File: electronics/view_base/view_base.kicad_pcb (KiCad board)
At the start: 2 copper layers, 81.2 x 81.2 mm, 111 parts, among them J1 BLDC, J2 USB_C_Receptacle_USB2.0, J3 LCD, J4 A, J5 B, J6 Conn_01x28_Socket, J7 Conn_01x28_Socket, J8 Conn_01x03_Socket, J9 Conn_01x04_Socket, Q1 MMBT4403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

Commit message: sunday work
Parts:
- moved J8 229.9 mm to (88.5, 192.0)
- moved J6 193.5 mm to (71.0, 155.8)
- moved J7 193.5 mm to (75.6, 155.8)
- moved J9 191.9 mm to (102.5, 153.0)
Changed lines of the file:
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@@
 		(legacy_teardrops no)
 	)
-	(paper "A4")
+	(paper "A3")
 	(layers
 		(0 "F.Cu" signal)
@@
 	(footprint "Connector_PinSocket_2.54mm:PinSocket_1x28_P2.54mm_Vertical"
 		(layer "F.Cu")
-		(at 66.2 -37.58)
+		(at 71 155.84)
 		(descr "Through hole straight socket strip, 1x28, 2.54mm pitch, single row (from Kicad 4.0.7), script generated")
 		(tags "Through hole socket strip THT 1x28 2.54mm single row")
@@
 	(footprint "Connector_PinSocket_2.54mm:PinSocket_1x28_P2.54mm_Vertical"
 		(layer "F.Cu")
-		(at 70.8 -37.58)
+		(at 75.6 155.84)
 		(descr "Through hole straight socket strip, 1x28, 2.54mm pitch, single row (from Kicad 4.0.7), script generated")
 		(tags "Through hole socket strip THT 1x28 2.54mm single row")
@@
 	(footprint "Connector_PinSocket_2.54mm:PinSocket_1x03_P2.54mm_Vertical"
 		(layer "F.Cu")
-		(at 75.4 -37.58)
+		(at 88.5 191.96)
 		(descr "Through hole straight socket strip, 1x03, 2.54mm pitch, single row (from Kicad 4.0.7), script generated")
 		(tags "Through hole socket strip THT 1x03 2.54mm single row")
@@
 	(footprint "Connector_PinSocket_2.54mm:PinSocket_1x04_P2.54mm_Vertical"
 		(layer "F.Cu")
-		(at 80 -37.58)
+		(at 102.5 152.96)
 		(descr "Through hole straight socket strip, 1x04, 2.54mm pitch, single row (from Kicad 4.0.7), script generated")
 		(tags "Through hole socket strip THT 1x04 2.54mm single row")
@@
 	(gr_arc
 		(start 103.499999 116.00781)
-		(mid 103.605914 115.700081)
+		(mid 103.60591 115.700076)
 		(end 103.878787 115.522725)
 		(stroke
@@
 	(gr_arc
 		(start 114.716361 102.903226)
-		(mid 114.889406 102.613745)
+		(mid 114.889406 102.613747)
 		(end 115.206906 102.5)
 		(stroke
@@
 	(gr_arc
 		(start 115.522726 103.878787)
-		(mid 115.700082 103.605915)
+		(mid 115.700083 103.605919)
 		(end 116.00781 103.5)
 		(stroke
@@
 	(gr_arc
 		(start 123.290199 96.500001)
-		(mid 123.790199 97.000001)
+		(mid 123.790199 97)
 		(end 123.290199 97.500001)
 		(stroke
@@
 	(gr_arc
 		(start 106.999999 97.250001)
-		(mid 107.219669 96.719671)
+		(mid 107.219668 96.71967)
 		(end 107.749999 96.500001)
 		(stroke
@@
 	(gr_arc
 		(start 107.749999 103.5)
-		(mid 107.219669 103.28033)
+		(mid 107.21967 103.28033)
 		(end 106.999999 102.75)
 		(stroke
@@
 	(gr_arc
 		(start 115.206906 97.500002)
-		(mid 114.889405 97.386257)
+		(mid 114.889401 97.38626)
 		(end 114.71636 97.096775)
 		(stroke
@@
 	(gr_arc
 		(start 102.499998 115.206906)
-		(mid 102.613743 114.889405)
+		(mid 102.61374 114.889401)
 		(end 102.903225 114.71636)
 		(stroke
@@
 	(gr_arc
 		(start 140.6 136.599999)
-		(mid 139.428427 139.428426)
+		(mid 139.428427 139.428427)
 		(end 136.6 140.599999)
 		(stroke
@@
 	(gr_arc
 		(start 76.709801 103.499999)
-		(mid 76.209801 102.999999)
+		(mid 76.209801 103)
 		(end 76.709801 102.499999)
 		(stroke
@@
 	(gr_arc
 		(start 83.99219 103.499999)
-		(mid 84.299919 103.605914)
+		(mid 84.299924 103.60591)
 		(end 84.477275 103.878787)
 		(stroke
@@
 	(gr_arc
 		(start 97.096774 114.71636)
-		(mid 97.386256 114.889405)
+		(mid 97.386254 114.889406)
 		(end 97.500001 115.206906)
 		(stroke
@@
 	(gr_arc
 		(start 84.793094 102.499998)
-		(mid 85.110595 102.613743)
+		(mid 85.110599 102.61374)
 		(end 85.28364 102.903225)
 		(stroke
@@
 	(gr_arc
 		(start 102.903226 85.283639)
-		(mid 102.613745 85.110594)
+		(mid 102.613747 85.110594)
 		(end 102.5 84.793094)
 		(stroke
@@
 	(gr_arc
 		(start 123.290199 102.5)
-		(mid 123.790199 103)
+		(mid 123.7902 103)
 		(end 123.290199 103.5)
 		(stroke
@@
 	(gr_arc
 		(start 96.121213 115.522726)
-		(mid 96.394085 115.700082)
+		(mid 96.394081 115.700083)
 		(end 96.5 116.00781)
 		(stroke
@@
 	(gr_arc
 		(start 97.500002 84.793094)
-		(mid 97.386257 85.110595)
+		(mid 97.38626 85.110599)
 		(end 97.096775 85.28364)
 		(stroke
@@
 	(gr_arc
 		(start 103.878787 84.477274)
-		(mid 103.605915 84.299918)
+		(mid 103.605919 84.299917)
 		(end 103.5 83.99219)
 		(stroke
@@
 	(gr_arc
 		(start 116.00781 96.500001)
-		(mid 115.700081 96.394086)
+		(mid 115.700076 96.39409)
 		(end 115.522725 96.121213)
 		(stroke
@@
 	(gr_arc
 		(start 96.500001 83.99219)
-		(mid 96.394086 84.299919)
+		(mid 96.39409 84.299924)
 		(end 96.121213 84.477275)
 		(stroke
@@
 	(gr_arc
 		(start 76.709801 97.5)
-		(mid 76.209801 97)
+		(mid 76.2098 97)
 		(end 76.709801 96.5)
 		(stroke
@@
 	(gr_arc
 		(start 85.283638 97.096775)
-		(mid 85.110593 97.386256)
+		(mid 85.110593 97.386253)
 		(end 84.793094 97.5)
 		(stroke
@@
 	(gr_arc
 		(start 84.477274 96.121213)
-		(mid 84.299918 96.394085)
+		(mid 84.299917 96.394081)
 		(end 83.99219 96.5)
 		(stroke

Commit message: initial layout
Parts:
- removed C28: 1uF, Capacitor_SMD:C_0603_1608Metric
- removed R17: 10k, Resistor_SMD:R_0603_1608Metric
- removed U2: T-Micro32_Plus, lilygo_micro32:T-Micro32
- moved J8 145.4 mm to (53.7, 50.8), turned to 180 degrees
- moved J9 119.8 mm to (35.9, 53.4), turned to 180 degrees
- moved J7 43.9 mm to (35.9, 137.2), turned to 180 degrees
- moved J6 25.5 mm to (53.7, 137.2), turned to 180 degrees
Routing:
- net /SCL: track 104.2 -> 0.00 mm, vias 4 -> 0
- net /GPIO12: track 0.00 -> 104.2 mm, vias 0 -> 4
- net /SDA: track 97.0 -> 0.00 mm, vias 3 -> 0
- net /GPIO13: track 0.00 -> 97.0 mm, vias 0 -> 3
- net /TMC_DIAG: track 85.9 -> 0.00 mm
- net /GPIO0: track 0.00 -> 85.9 mm
- net /TMC_VL: track 75.2 -> 0.00 mm, vias 2 -> 0
- net /GPIO1: track 0.00 -> 75.2 mm, vias 0 -> 2
- net /TMC_WL: track 71.5 -> 0.00 mm, vias 2 -> 0
- net /GPIO2: track 0.00 -> 71.5 mm, vias 0 -> 2
- net /TMC_UL: track 68.4 -> 0.00 mm, vias 2 -> 0
- net /GPIO3: track 0.00 -> 68.4 mm, vias 0 -> 2
- net /TMC_WH: track 68.0 -> 0.00 mm, vias 4 -> 0
- net /GPIO7: track 0.00 -> 68.0 mm, vias 0 -> 4
- net /TMC_VH: track 67.3 -> 0.00 mm, vias 4 -> 0
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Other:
- board size 81.2 x 81.2 mm -> 110.1 x 100 mm

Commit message: more layout and simplification
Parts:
- removed Q2: UMH3N, Package_TO_SOT_SMD:SOT-363_SC-70-6
- removed TP13: EN, Modified:TestPoint_Pad_D2.0mm_ValueSilk
- removed TP14: BOOT, Modified:TestPoint_Pad_D2.0mm_ValueSilk
- moved C26 45.3 mm to (58.0, 73.0), turned to 90 degrees
- moved J3 41.1 mm to (58.0, 79.0)
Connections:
- J6 pad 18: /ESP32_BOOT -> /GPIO15
- R12 pad 1: /GPIO1 -> /GPIO21
- U3 pad 13: /DTR -> unconnected-(U3-~{DTR}-Pad13)
- U3 pad 14: /RTS -> unconnected-(U3-~{RTS}-Pad14)
- U3 pad 2: /GPIO21 -> unconnected-(U3-TXD-Pad2)
- U3 pad 3: /GPIO22 -> unconnected-(U3-RXD-Pad3)
- U5 pad 10: /GPIO1 -> /GPIO21
- U5 pad 12: /GPIO0 -> /GPIO20
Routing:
- net /GPIO20: track 4.41 -> 85.9 mm, vias 1 -> 0
- net /GPIO21: track 22.8 -> 98.0 mm, vias 2 -> 4
- net GND: track 68.3 -> 136.5 mm, vias 46 -> 45
- net +5V: track 256.1 -> 321.0 mm
- net +3V3: track 331.0 -> 381.8 mm, vias 14 -> 16
- net /SWD: track 0.00 -> 29.6 mm
- net /SWCLK: track 0.00 -> 28.6 mm, vias 0 -> 2
- net /DTR: track 17.4 -> 0.00 mm, vias 2 -> 0
- net /RTS: track 16.4 -> 0.00 mm
- net /GPIO1: track 75.2 -> 81.0 mm, vias 2 -> 0
- net /GPIO19: track 4.41 -> 0.00 mm, vias 1 -> 0
- net /GPIO18: track 4.41 -> 0.00 mm, vias 1 -> 0
- net /GPIO0: track 85.9 -> 90.1 mm, vias 0 -> 1
- net /GPIO23: track 4.00 -> 0.00 mm, vias 1 -> 0
- net /GPIO17: track 4.00 -> 0.00 mm, vias 1 -> 0
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
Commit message: more layout
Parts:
- removed TP15: TX, Modified:TestPoint_Pad_D2.0mm_ValueSilk
- removed TP16: RX, Modified:TestPoint_Pad_D2.0mm_ValueSilk
- moved J3 2.00 mm to (58.0, 77.0)
- moved C26 0.50 mm to (58.0, 72.5)
- moved C25 0.22 mm to (79.0, 135.2)
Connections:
- J3 pad 3: /GPIO16 -> /GPIO21
- J3 pad 4: /GPIO17 -> /GPIO20
- J3 pad 5: /GPIO18 -> /GPIO19
- J3 pad 6: /GPIO19 -> /GPIO18
- J3 pad 7: /GPIO20 -> /GPIO17
- J3 pad 8: /GPIO23 -> /GPIO16
- R10 pad 1: /GPIO3 -> /TMC_UL
- R11 pad 1: /GPIO2 -> /TMC_WL
- U3 pad 2: unconnected-(U3-TXD-Pad2) -> /GPIO3
- U3 pad 3: unconnected-(U3-RXD-Pad3) -> /GPIO2
- U4 pad 11: /GPIO14 -> /GPIO23
- U4 pad 12: /GPIO10 -> /GPIO22
- U5 pad 12: /GPIO20 -> /GPIO4
- U5 pad 6: /GPIO3 -> /TMC_UL
- U5 pad 7: /GPIO2 -> /TMC_WL
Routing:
- net /GPIO4: track 67.1 -> 176.3 mm
- net /GPIO20: track 85.9 -> 5.03 mm
- net /TMC_WL: track 0.00 -> 71.5 mm, vias 0 -> 2
- net /TMC_UL: track 0.00 -> 68.4 mm, vias 0 -> 2
- net /GPIO10: track 55.3 -> 0.00 mm, vias 2 -> 0
- net /GPIO14: track 54.5 -> 0.00 mm, vias 2 -> 0
- net /GPIO2: track 71.5 -> 34.3 mm, vias 2 -> 0
- net /GPIO3: track 68.4 -> 34.8 mm, vias 2 -> 0
- net /GPIO21: track 98.0 -> 80.5 mm, vias 4 -> 2
- net /GPIO23: track 0.00 -> 14.5 mm, vias 0 -> 2
- net /GPIO22: track 23.0 -> 14.3 mm
- net +3V3: track 381.8 -> 374.5 mm, vias 16 -> 12
- net /GPIO19: track 0.00 -> 4.81 mm
- net /GPIO18: track 0.00 -> 4.59 mm
- net /GPIO16: track 0.00 -> 4.52 mm
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
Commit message: worked on some routing and edited the ground plane, feel free to revert just wanted to mess with it
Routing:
- net /GPIO21: track 80.5 -> 138.1 mm, vias 2 -> 3
- net /GPIO8: track 47.0 -> 79.6 mm, vias 1 -> 3
- net /GPIO9: track 48.7 -> 79.9 mm, vias 1 -> 3
- net /GPIO11: track 4.40 -> 33.5 mm, vias 0 -> 2
- net /GPIO5: track 67.3 -> 95.3 mm, vias 4 -> 6
- net /GPIO6: track 52.2 -> 79.2 mm, vias 1 -> 3
- net /GPIO7: track 68.0 -> 94.5 mm, vias 4 -> 6
- net /GPIO12: track 104.2 -> 129.7 mm, vias 2 -> 4
- net /GPIO13: track 97.0 -> 112.2 mm, vias 1 -> 3
- net /GPIO0: track 90.1 -> 92.0 mm
- net /SWD: track 29.6 -> 28.5 mm
- net GND: track 134.6 -> 134.3 mm, vias 44 -> 45

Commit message: got rid of some ground traces in favor of using plane
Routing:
- net GND: track 134.3 -> 64.9 mm, vias 45 -> 44
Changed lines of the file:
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@@
-	)
-	(segment
-		(start 32 64.71)
-		(end 32 45)
-		(width 0.15)
-		(layer "F.Cu")
-		(net 1)
 	)
 	(segment
@@
 	)
 	(segment
-		(start 35.89 68.6)
-		(end 32 64.71)
-		(width 0.15)
-		(layer "F.Cu")
-		(net 1)
-	)
-	(segment
 		(start 115.24834 91.356108)
 		(end 114.322236 90.430004)
@@
 	)
 	(segment
-		(start 32 45)
-		(end 34 43)
-		(width 0.15)
-		(layer "F.Cu")
-		(net 1)
-	)
-	(segment
 		(start 68 109.5)
 		(end 68.5 109.5)
@@
 	)
 	(segment
-		(start 34 43)
-		(end 48.39 43)
-		(width 0.15)
-		(layer "F.Cu")
-		(net 1)
-	)
-	(segment
 		(start 126.55 120.908226)
 		(end 125.989142 120.347368)
@@
 	)
 	(segment
-		(start 32.305 44.695)
-		(end 34 43)
-		(width 0.15)
-		(layer "F.Cu")
-		(net 1)
-	)
-	(segment
 		(start 124.025 122.8)
 		(end 124 122.775)
@@
 	(via
 		(at 120 139.5)
-		(size 0.8)
-		(drill 0.4)
-		(layers "F.Cu" "B.Cu")
-		(net 1)
-	)
-	(via
-		(at 48.39 43)
 		(size 0.8)
 		(drill 0.4)
@@
 		(width 0.15)
 		(layer "B.Cu")
-		(net 1)
-	)
-	(segment
-		(start 53.67 48.28)
-		(end 58.9 53.51)
-		(width 0.15)
-		(layer "B.Cu")
-		(net 1)
-	)
-	(segment
-		(start 53.67 48.28)
-		(end 48.39 43)
-		(width 0.15)
-		(layer "B.Cu")
-		(net 1)
-	)
-	(segment
-		(start 58.9 53.51)
-		(end 58.9 58.9)
-		(width 0.15)
-		(layer "B.Cu")
-		(net 1)
-	)
-	(segment
-		(start 58.9 58.9)
-		(end 62 62)
-		(width 0.15)
-		(layer "B.Cu")

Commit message: finished layout
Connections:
- R10 pad 1: /TMC_UL -> /GPIO7
- R11 pad 1: /TMC_WL -> /GPIO6
- R12 pad 1: /GPIO21 -> /GPIO5
- R13 pad 2: /GPIO13 -> /GPIO24
- R14 pad 2: /GPIO12 -> /GPIO15
- R15 pad 2: /GPIO9 -> /GPIO14
- R16 pad 1: /GPIO8 -> /GPIO13
- R7 pad 1: /GPIO4 -> /GPIO8
- R8 pad 1: /GPIO5 -> /GPIO9
- R9 pad 1: /GPIO7 -> /GPIO10
- TP10 pad 1: /GPIO8 -> /GPIO13
- TP11 pad 1: /GPIO9 -> /GPIO14
- TP4 pad 1: /GPIO13 -> /GPIO24
- TP5 pad 1: /GPIO12 -> /GPIO15
- TP9 pad 1: /GPIO6 -> /GPIO12
- U1 pad 6: /GPIO9 -> /GPIO14
- U1 pad 7: /GPIO8 -> /GPIO13
- U1 pad 8: /GPIO6 -> /GPIO12
- U5 pad 10: /GPIO21 -> /GPIO5
- U5 pad 3: /GPIO4 -> /GPIO8
- U5 pad 4: /GPIO5 -> /GPIO9
- U5 pad 5: /GPIO7 -> /GPIO10
- U5 pad 6: /TMC_UL -> /GPIO7
- U5 pad 7: /TMC_WL -> /GPIO6
- U8 pad 1: /GPIO12 -> /GPIO15
- U8 pad 4: /GPIO13 -> /GPIO24
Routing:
- net /GPIO21: track 138.1 -> 5.26 mm, vias 3 -> 0
- net /GPIO15: track 0.00 -> 100.9 mm, vias 0 -> 3
- net /GPIO10: track 0.00 -> 97.2 mm, vias 0 -> 4
- net /GPIO24: track 0.00 -> 91.1 mm, vias 0 -> 1
- net /TMC_WL: track 71.5 -> 0.00 mm, vias 2 -> 0
- net /TMC_UL: track 68.4 -> 0.00 mm, vias 2 -> 0
- net /GPIO4: track 176.3 -> 109.1 mm, vias 4 -> 0
- net /GPIO14: track 0.00 -> 65.7 mm, vias 0 -> 2
- net /GPIO12: track 129.7 -> 64.9 mm, vias 4 -> 2
- net /GPIO13: track 112.2 -> 66.1 mm, vias 3 -> 2
- net /GPIO6: track 79.2 -> 98.5 mm, vias 3 -> 2
- net /GPIO9: track 79.9 -> 96.2 mm, vias 3 -> 4
- net /GPIO8: track 79.6 -> 95.5 mm, vias 3 -> 4
- net /GPIO11: track 33.5 -> 21.7 mm, vias 2 -> 0
- net /GPIO5: track 95.3 -> 101.5 mm, vias 6 -> 2
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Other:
- board size 110.1 x 100 mm -> 110.1 x 99.8 mm

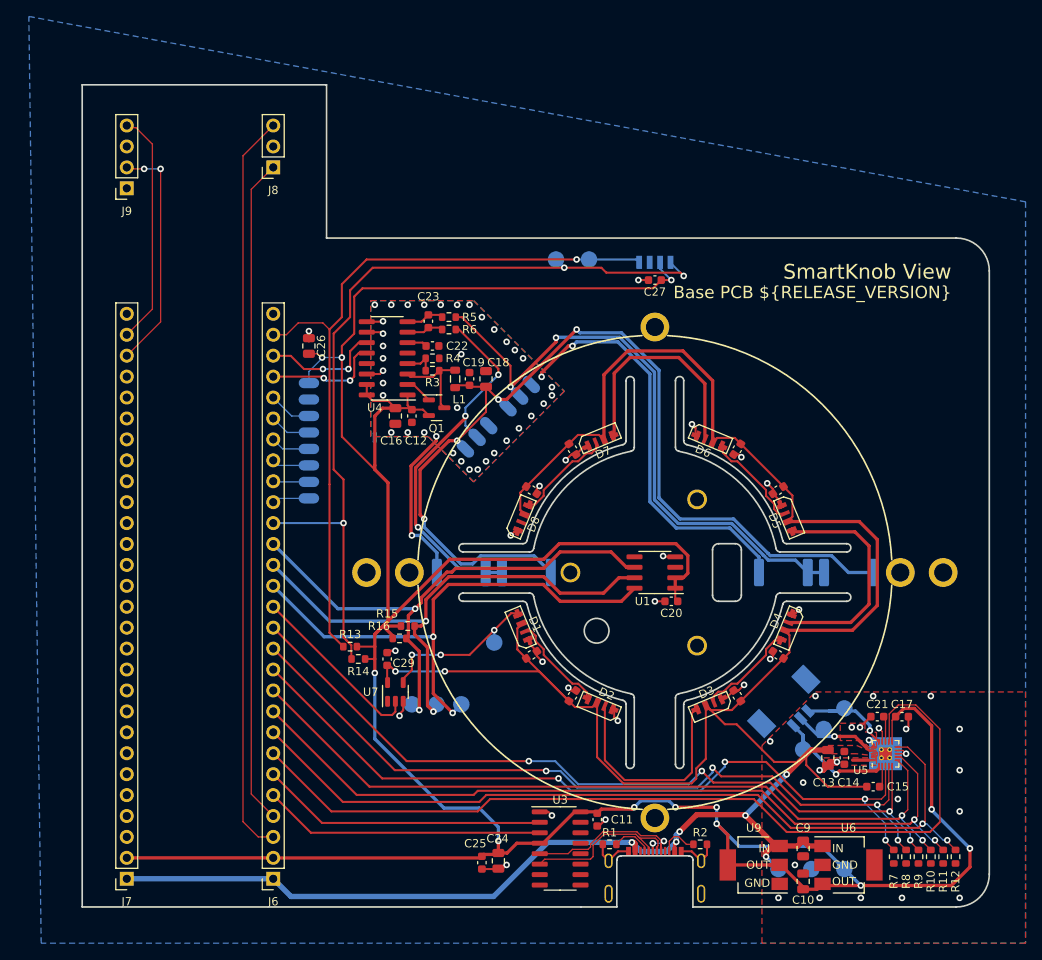
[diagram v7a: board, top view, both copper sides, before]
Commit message: redid routing and schematic to match GPIO pins from excel
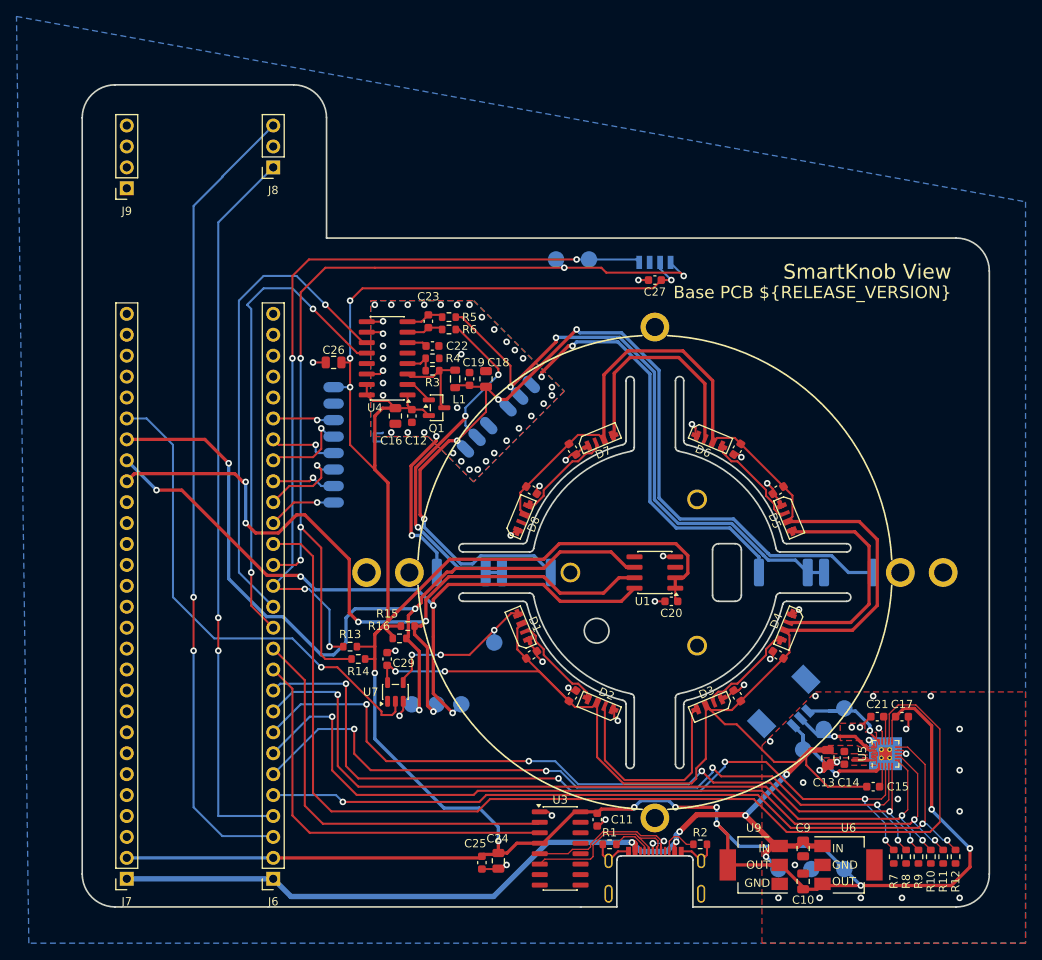
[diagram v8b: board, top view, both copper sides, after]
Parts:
- moved C26 3.61 mm to (61.0, 74.5), turned to 180 degrees
- moved J3 3.04 mm to (61.0, 77.5)
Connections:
- J3 pad 3: /GPIO21 -> /GPIO20
- J3 pad 4: /GPIO20 -> /GPIO18
- J3 pad 6: /GPIO18 -> /GPIO16
- J3 pad 8: /GPIO16 -> /GPIO15
- J9 pad 2: /SWCLK -> unconnected-(J9-Pin_2-Pad2)
- J9 pad 4: /SWD -> unconnected-(J9-Pin_4-Pad4)
- R10 pad 1: /GPIO7 -> /GPIO6
- R11 pad 1: /GPIO6 -> /GPIO4
- R12 pad 1: /GPIO5 -> /GPIO2
- R13 pad 2: /GPIO24 -> /GPIO12
- R14 pad 2: /GPIO15 -> /GPIO13
- R15 pad 2: /GPIO14 -> /GPIO28
- R16 pad 1: /GPIO13 -> /GPIO30
- R7 pad 1: /GPIO8 -> /GPIO7
- R8 pad 1: /GPIO9 -> /GPIO3
- R9 pad 1: /GPIO10 -> /GPIO5
- TP10 pad 1: /GPIO13 -> /GPIO30
- TP11 pad 1: /GPIO14 -> /GPIO28
- TP4 pad 1: /GPIO24 -> /GPIO12
- TP5 pad 1: /GPIO15 -> /GPIO13
- TP9 pad 1: /GPIO12 -> /GPIO29
- U1 pad 6: /GPIO14 -> /GPIO28
- U1 pad 7: /GPIO13 -> /GPIO30
- U1 pad 8: /GPIO12 -> /GPIO29
- U3 pad 2: /GPIO3 -> /GPIO9
- U3 pad 3: /GPIO2 -> /GPIO8
- U4 pad 11: /GPIO23 -> /GPIO11
- U4 pad 12: /GPIO22 -> /GPIO10
- U5 pad 10: /GPIO5 -> /GPIO2
- U5 pad 12: /GPIO4 -> /GPIO14
- U5 pad 3: /GPIO8 -> /GPIO7
- U5 pad 4: /GPIO9 -> /GPIO3
- U5 pad 5: /GPIO10 -> /GPIO5
- U5 pad 6: /GPIO7 -> /GPIO6
- U5 pad 7: /GPIO6 -> /GPIO4
- U7 pad 2: /GPIO11 -> /GPIO27
- U8 pad 1: /GPIO15 -> /GPIO13
- U8 pad 4: /GPIO24 -> /GPIO12
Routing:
- net /GPIO28: track 0.00 -> 103.3 mm, vias 0 -> 3
- net /GPIO30: track 0.00 -> 97.5 mm, vias 0 -> 5
- net /GPIO15: track 100.9 -> 8.37 mm, vias 3 -> 1
- net /GPIO24: track 91.1 -> 0.00 mm, vias 1 -> 0
- net /GPIO29: track 0.00 -> 87.4 mm, vias 0 -> 4
- net /GPIO14: track 65.7 -> 136.5 mm, vias 2 -> 0
- net /GPIO2: track 34.3 -> 98.3 mm, vias 0 -> 3
- net /GPIO3: track 34.8 -> 96.2 mm, vias 0 -> 5
- net /GPIO27: track 0.00 -> 60.0 mm, vias 0 -> 1
- net /GPIO9: track 96.2 -> 50.2 mm, vias 4 -> 0
- net /GPIO8: track 95.5 -> 49.6 mm, vias 4 -> 0
- net /GPIO13: track 66.1 -> 108.5 mm, vias 2 -> 5
- net /GPIO10: track 97.2 -> 59.1 mm, vias 4 -> 2
- net /GPIO11: track 21.7 -> 59.0 mm, vias 0 -> 1
- net /GPIO12: track 64.9 -> 96.4 mm, vias 2 -> 4
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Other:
- outline, holes or cut-outs redrawn
